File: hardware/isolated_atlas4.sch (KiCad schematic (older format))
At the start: 14 parts, among them J601 CONN_01X02, U601 adm3260, U602 ATLAS_SENSOR

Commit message: Fix SSOP-20 width on the isolator.
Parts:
- U601: footprint SMD_Packages:SSOP-20 -> conservify:SSOP20-53
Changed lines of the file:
@@
 F 0 "U601" H 4400 2750 60  0000 C CNN
 F 1 "adm3260" H 4400 2900 60  0000 C CNN
-F 2 "SMD_Packages:SSOP-20" H 4400 2900 60  0001 C CNN
+F 2 "conservify:SSOP20-53" H 4400 2900 60  0001 C CNN
 F 3 "" H 4400 2900 60  0001 C CNN
 F 4 "584-ADM3260ARSZ" H 0   0   50  0001 C CNN "spn1"

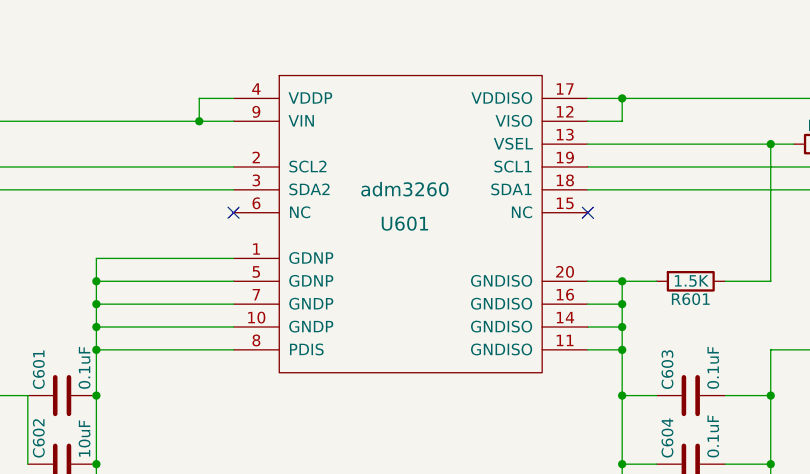
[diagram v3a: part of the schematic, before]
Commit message: Fixing some component names.
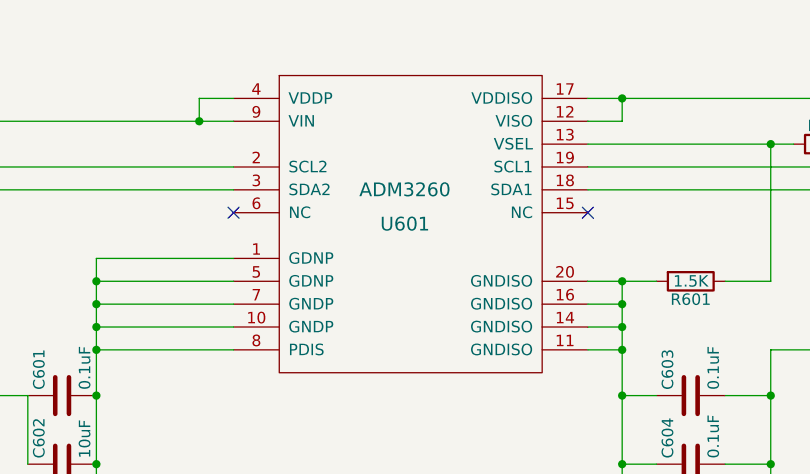
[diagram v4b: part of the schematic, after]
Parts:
- C601, C602, C603, C604, C605, C606, J601, R601, R602, R603, R604, R605, U602: price (none) -> 0
- U601: value adm3260 -> ADM3260; price (none) -> 0

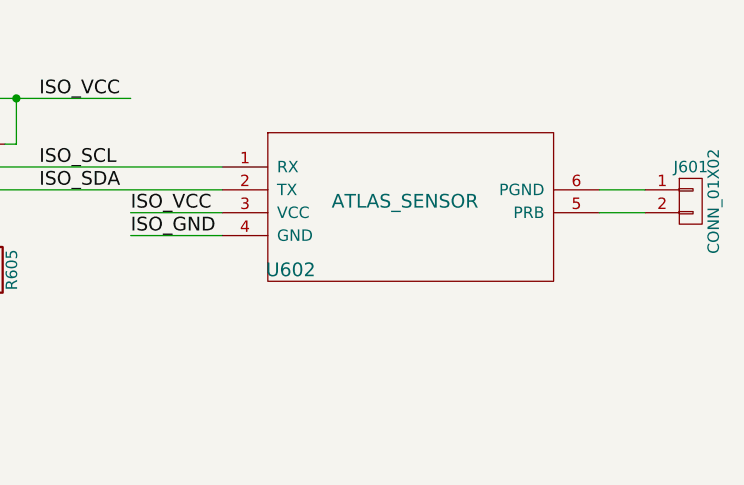
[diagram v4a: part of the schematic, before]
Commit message: Individual atlas sensor values for costing.
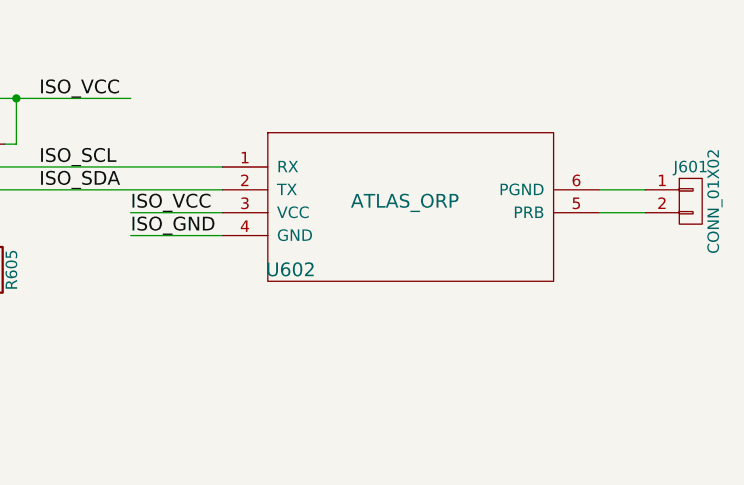
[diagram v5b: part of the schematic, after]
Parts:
- U602: value ATLAS_SENSOR -> ATLAS_ORP

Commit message: Normalizing some passive footprints.
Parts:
- C601, C603, C604: footprint Resistors_SMD:R_0603_HandSoldering -> Capacitors_SMD:C_0603_HandSoldering
- C602, C605, C606: footprint Resistors_SMD:R_0603_HandSoldering -> Capacitors_SMD:C_0603_HandSoldering; spn1 810-C1608X7S0J106M -> 81-GRM188R60J106ME47

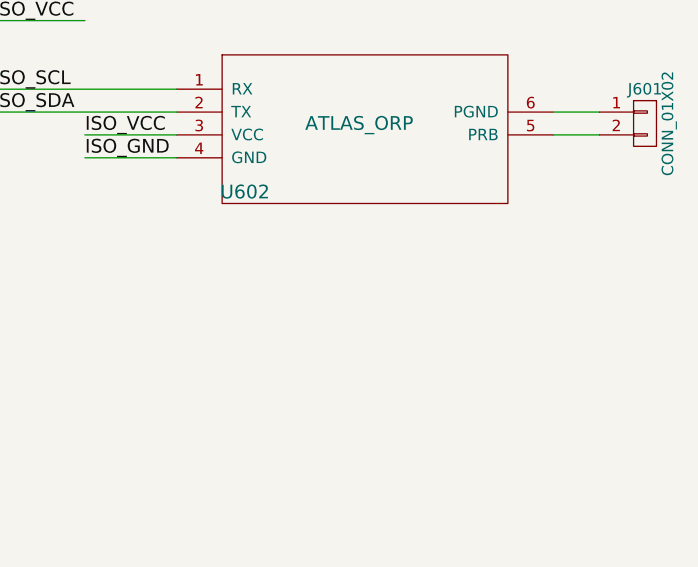
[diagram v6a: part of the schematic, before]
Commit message: Adding placeholders for probes for the BOM.
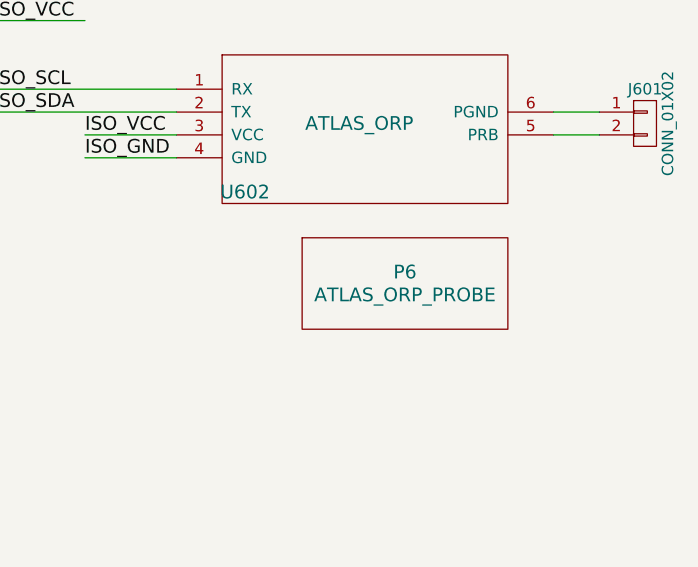
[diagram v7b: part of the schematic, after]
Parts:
- added P6: ATLAS_ORP_PROBE, Oddities:Dummy_Empty, symbol WATER_PROBE

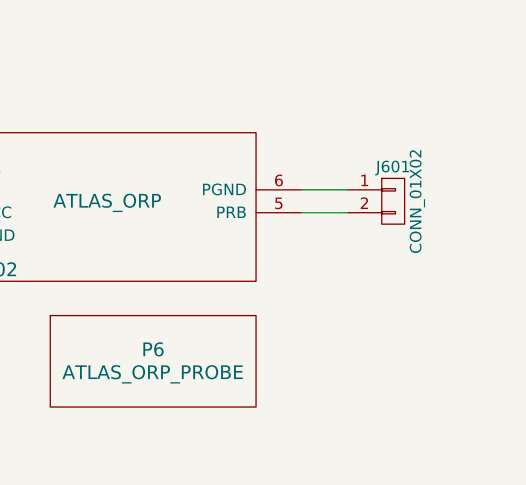
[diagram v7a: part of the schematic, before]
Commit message: Add footprint for OEM Atlas Circuit.
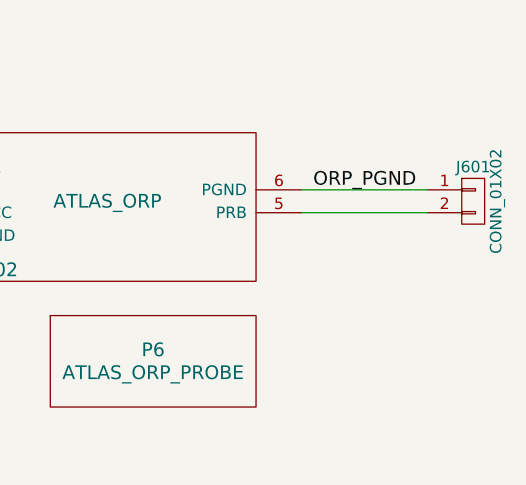
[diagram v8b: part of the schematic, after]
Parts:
- U602: footprint conservify:atlas_sensor_board -> conservify:ATLAS_SENSOR_BOARD_COMBO
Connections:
- net labels added: ORP_PGND
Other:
- moved on the sheet: J601
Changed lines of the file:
@@
 F 0 "U602" H 8100 2550 60  0000 C CNN
 F 1 "ATLAS_ORP" H 8600 2850 60  0000 C CNN
-F 2 "conservify:atlas_sensor_board" H 8550 2900 60  0001 C CNN
+F 2 "conservify:ATLAS_SENSOR_BOARD_COMBO" H 8550 2900 60  0001 C CNN
 F 3 "" H 8550 2900 60  0001 C CNN
 F 4 "0" H 8100 2650 50  0001 C CNN "price"
@@
 L CONN_01X02 J601
 U 1 1 59A1BC7E
-P 9850 2950
-F 0 "J601" H 9850 3100 50  0000 C CNN
-F 1 "CONN_01X02" V 9950 2950 50  0000 C CNN
-F 2 "conservify:BNC" H 9850 2950 50  0001 C CNN
-F 3 "" H 9850 2950 50  0001 C CNN
-F 4 "0" H 9850 3200 50  0001 C CNN "price"
-F 5 "523-31-5431" H 0   0   50  0001 C CNN "spn1"
-	1    9850 2950
+P 10200 2950
+F 0 "J601" H 10200 3100 50  0000 C CNN
+F 1 "CONN_01X02" V 10300 2950 50  0000 C CNN
+F 2 "conservify:BNC" H 10200 2950 50  0001 C CNN
+F 3 "" H 10200 2950 50  0001 C CNN
+F 4 "0" H 10200 3200 50  0001 C CNN "price"
+F 5 "523-31-5431" H 350 0   50  0001 C CNN "spn1"
+	1    10200 2950
 	1    0    0    -1
 $EndComp
@@
 	7400 3000 7800 3000
 Wire Wire Line
-	9650 2900 9450 2900
+	9450 2900 10000 2900
 Wire Wire Line
-	9450 3000 9650 3000
+	9450 3000 10000 3000
 Connection ~ 5350 3500
 Connection ~ 5350 3400
@@
 	1    0    0    -1
 $EndComp
+Text Label 9500 2900 0    60   ~ 0
+ORP_PGND
 $EndSCHEMATC
